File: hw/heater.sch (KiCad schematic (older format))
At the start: 12 parts, among them Q801 VNB35NV04TR-E, U802 VN5E010AH, U803 VN5E010AH, U804 MOSFET_P_ZXMP10A13F, U805 MOSFET-N_2N7002W

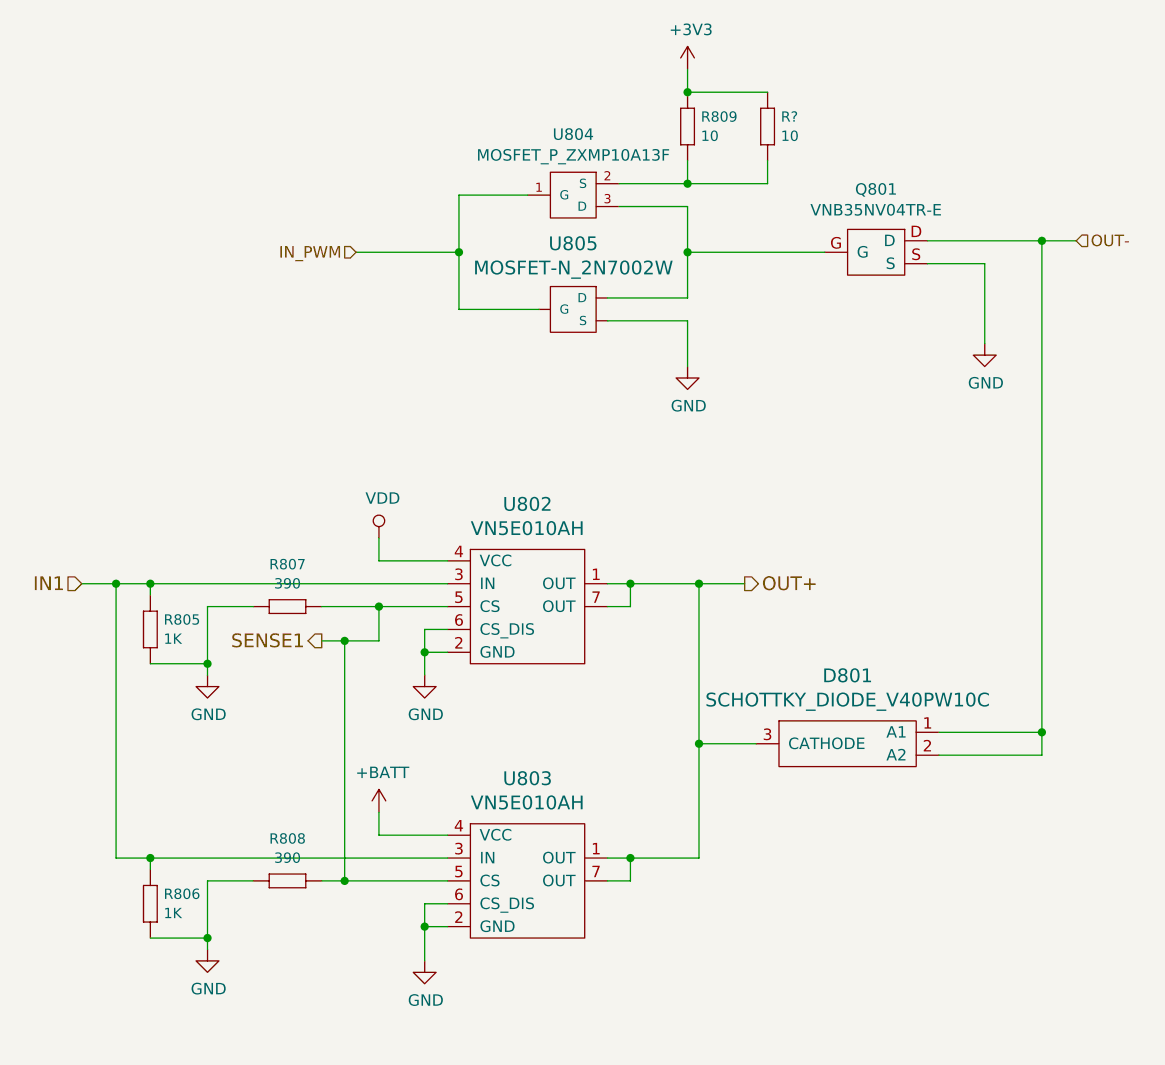
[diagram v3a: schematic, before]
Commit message: HAL updated to latest uv bootloader, starting to draw 6.0.0 pcb
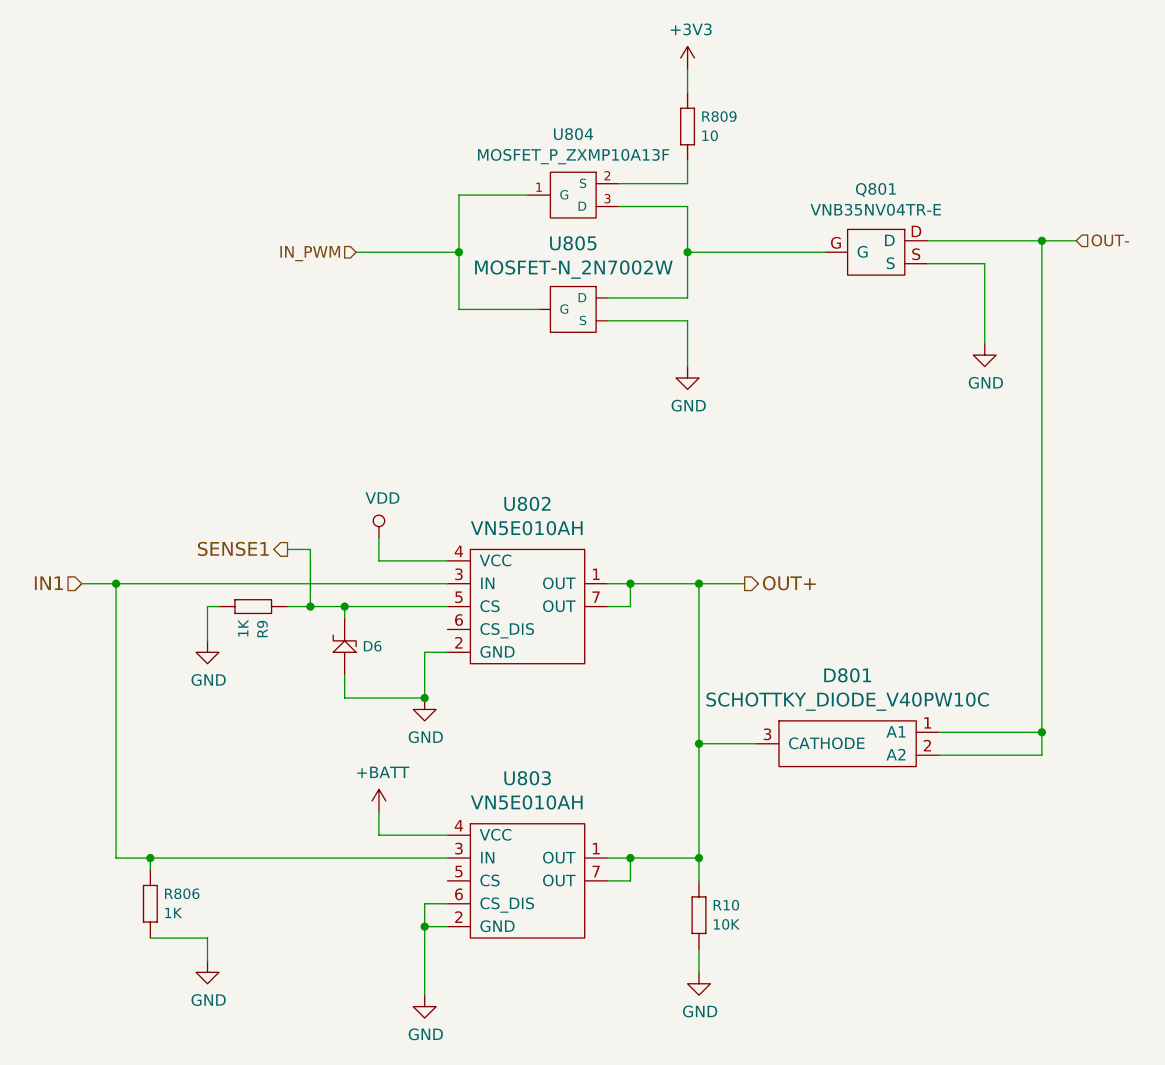
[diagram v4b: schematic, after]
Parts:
- removed R805: 1K, yageo:0603, symbol fsb-rescue:1K
- removed R807, R808: 390, yageo:0603, symbol fsb-rescue:390
- removed R?: 10, yageo:0603, symbol yageo:10
- added D6: ZENER_MM3Z3V6T1G, usevolt:SOD-323, symbol usevolt:ZENER_MM3Z3V6T1G
- added R10: 10K, yageo:0603, symbol fsb-rescue:10K
- added R9: 1K, yageo:0603, symbol fsb-rescue:1K
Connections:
- net GND: now also D6.2, R10.1 (R1), R9.1 (R1); no longer U802.6 (CS_DIS)
- net OUT+: now also R10.2 (R2)
- net SENSE1: now also D6.1, R9.2 (R2); no longer U803.5 (CS)
